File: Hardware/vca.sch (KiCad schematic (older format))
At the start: 41 parts, among them Q1 MMBFJ177, Q2 MMBFJ177, Q3 MMBFJ177, Q4 MMBFJ177, SW1 SW_DPDT_x2, SW2 SW_DPDT_x2, U4 TL074

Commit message: change GNDA to GND nets everywhere. Not using any ADC, so don't need separate digital and analog grounds.
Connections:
- net GNDA is gone; now on net GND: Q1.2 (S), Q2.2 (S), Q3.2 (S), Q4.2 (S), R?.1, R?.1, R?.1, R?.1
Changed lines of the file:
@@
-$EndComp
-$Comp
-L GNDA #PWR37
-U 1 1 5C359DD5
-P 4550 1600
-F 0 "#PWR37" H 4550 1350 50  0001 C CNN
-F 1 "GNDA" H 4550 1450 50  0000 C CNN
-F 2 "" H 4550 1600 50  0001 C CNN
-F 3 "" H 4550 1600 50  0001 C CNN
-	1    4550 1600
-	1    0    0    -1
 $EndComp
 $Comp
@@
 $EndComp
 $Comp
-L GNDA #PWR38
-U 1 1 5C36E8F0
-P 4550 3000
-F 0 "#PWR38" H 4550 2750 50  0001 C CNN
-F 1 "GNDA" H 4550 2850 50  0000 C CNN
-F 2 "" H 4550 3000 50  0001 C CNN
-F 3 "" H 4550 3000 50  0001 C CNN
-	1    4550 3000
-	1    0    0    -1
-$EndComp
-$Comp
 L R R34
 U 1 1 5C36E8F9
@@
 $EndComp
 $Comp
-L GNDA #PWR39
-U 1 1 5C36E9E8
-P 4550 4250
-F 0 "#PWR39" H 4550 4000 50  0001 C CNN
-F 1 "GNDA" H 4550 4100 50  0000 C CNN
-F 2 "" H 4550 4250 50  0001 C CNN
-F 3 "" H 4550 4250 50  0001 C CNN
-	1    4550 4250
-	1    0    0    -1
-$EndComp
-$Comp
 L R R35
 U 1 1 5C36E9F1
@@
 $EndComp
 $Comp
-L GNDA #PWR40
-U 1 1 5C36EAE0
-P 4550 5600
-F 0 "#PWR40" H 4550 5350 50  0001 C CNN
-F 1 "GNDA" H 4550 5450 50  0000 C CNN
-F 2 "" H 4550 5600 50  0001 C CNN
-F 3 "" H 4550 5600 50  0001 C CNN
-	1    4550 5600
-	1    0    0    -1
-$EndComp
-$Comp
 L R R36
 U 1 1 5C36EAE9
@@
 $EndComp
 $Comp
-L GNDA #PWR?
-U 1 1 5C37BC69
-P 6700 1450
-F 0 "#PWR?" H 6700 1200 50  0001 C CNN
-F 1 "GNDA" H 6700 1300 50  0000 C CNN
-F 2 "" H 6700 1450 50  0001 C CNN
-F 3 "" H 6700 1450 50  0001 C CNN
-	1    6700 1450
-	1    0    0    -1
-$EndComp
-$Comp
-L GNDA #PWR?
-U 1 1 5C37BCE0
-P 6700 2850
-F 0 "#PWR?" H 6700 2600 50  0001 C CNN
-F 1 "GNDA" H 6700 2700 50  0000 C CNN
-F 2 "" H 6700 2850 50  0001 C CNN
-F 3 "" H 6700 2850 50  0001 C CNN
-	1    6700 2850
-	1    0    0    -1
-$EndComp
-$Comp
-L GNDA #PWR?
-U 1 1 5C37BD57
-P 6700 4150
-F 0 "#PWR?" H 6700 3900 50  0001 C CNN
-F 1 "GNDA" H 6700 4000 50  0000 C CNN
-F 2 "" H 6700 4150 50  0001 C CNN
-F 3 "" H 6700 4150 50  0001 C CNN
-	1    6700 4150
-	1    0    0    -1
-$EndComp
-$Comp
-L GNDA #PWR?
-U 1 1 5C37BDCE
-P 6700 5450
-F 0 "#PWR?" H 6700 5200 50  0001 C CNN
-F 1 "GNDA" H 6700 5300 50  0000 C CNN
-F 2 "" H 6700 5450 50  0001 C CNN
-F 3 "" H 6700 5450 50  0001 C CNN
-	1    6700 5450
-	1    0    0    -1
-$EndComp
-$Comp
 L R R?
 U 1 1 5C3881CE
@@
 Connection ~ 4550 950
 Wire Wire Line
-	3200 1300 3350 1300
-Wire Wire Line
-	3350 1300 3450 1300
+	3200 1300 3450 1300
 Wire Wire Line
 	2900 1500 3450 1500
@@
 Connection ~ 4550 2350
 Wire Wire Line
-	3300 2700 3400 2700
-Wire Wire Line
-	3400 2700 3450 2700
+	3300 2700 3450 2700
 Wire Wire Line
 	2950 2900 3450 2900
@@
 Connection ~ 4550 3600
 Wire Wire Line
-	3200 3950 3350 3950
-Wire Wire Line
-	3350 3950 3450 3950
+	3200 3950 3450 3950
 Wire Wire Line
 	2850 4150 3450 4150
@@
 Connection ~ 4550 4950
 Wire Wire Line
-	3200 5300 3350 5300
-Wire Wire Line
-	3350 5300 3450 5300
+	3200 5300 3450 5300
 Wire Wire Line
 	2850 5500 3450 5500
@@
 Connection ~ 5150 2350
 Wire Wire Line
-	4250 950  4550 950
-Wire Wire Line
-	4550 950  4800 950
-Wire Wire Line
-	5000 950  5200 950
-Wire Wire Line
-	5200 950  5550 950
-Wire Wire Line
-	5000 2350 5150 2350
-Wire Wire Line
-	5150 2350 5550 2350
-Wire Wire Line
-	4250 2350 4550 2350
-Wire Wire Line
-	4550 2350 4800 2350
-Wire Wire Line
-	4250 3600 4550 3600
-Wire Wire Line
-	4550 3600 4800 3600
-Wire Wire Line
-	5000 3600 5150 3600
-Wire Wire Line
-	5150 3600 5550 3600
-Wire Wire Line
-	4250 4950 4550 4950
-Wire Wire Line
-	4550 4950 4800 4950
-Wire Wire Line
-	5000 4950 5150 4950
-Wire Wire Line
-	5150 4950 5550 4950
-Wire Wire Line
-	6150 1050 6300 1050
-Wire Wire Line
-	6300 1050 6450 1050
-Wire Wire Line
-	6650 1050 6700 1050
-Wire Wire Line
-	6700 1050 6800 1050
+	4250 950  4800 950
+Wire Wire Line
+	5000 950  5550 950
+Wire Wire Line
+	5000 2350 5550 2350
+Wire Wire Line
+	4250 2350 4800 2350
+Wire Wire Line
+	4250 3600 4800 3600
+Wire Wire Line
+	5000 3600 5550 3600
+Wire Wire Line
+	4250 4950 4800 4950
+Wire Wire Line
+	5000 4950 5550 4950
+Wire Wire Line
+	6150 1050 6450 1050
+Wire Wire Line
+	6650 1050 6800 1050
 Wire Wire Line
 	6700 1150 6700 1050
 Connection ~ 6700 1050
 Wire Wire Line
-	6150 2450 6300 2450
-Wire Wire Line
-	6300 2450 6450 2450
-Wire Wire Line
-	6650 2450 6700 2450
-Wire Wire Line
-	6700 2450 6800 2450
+	6150 2450 6450 2450
+Wire Wire Line
+	6650 2450 6800 2450
 Wire Wire Line
 	6700 2550 6700 2450
 Connection ~ 6700 2450
 Wire Wire Line
-	6150 3700 6300 3700
-Wire Wire Line
-	6300 3700 6450 3700
-Wire Wire Line
-	6650 3700 6700 3700
-Wire Wire Line
-	6700 3700 6800 3700
+	6150 3700 6450 3700
+Wire Wire Line
+	6650 3700 6800 3700
 Wire Wire Line
 	6700 3850 6700 3700
 Connection ~ 6700 3700
 Wire Wire Line
-	6150 5050 6300 5050
-Wire Wire Line
-	6300 5050 6450 5050
-Wire Wire Line
-	6650 5050 6700 5050
-Wire Wire Line
-	6700 5050 6800 5050
+	6150 5050 6450 5050
+Wire Wire Line
+	6650 5050 6800 5050
 Wire Wire Line
 	6700 5150 6700 5050
@@
 	1000 1550 1000 1550
 Wire Wire Line
-	1000 1150 1000 1200
-Wire Wire Line
-	1000 1200 1000 1250
+	1000 1150 1000 1250
 Wire Wire Line
 	1000 800  1000 850
@@
 Text Notes 550  2100 0    60   ~ 0
 Determine bias voltage \nunder test, or leave \nunloaded as needed.
+$Comp
+L GND #PWR?
+U 1 1 5C3BC4D7
+P 4550 1600
+F 0 "#PWR?" H 4550 1350 50  0001 C CNN
+F 1 "GND" H 4550 1450 50  0000 C CNN
+F 2 "" H 4550 1600 50  0001 C CNN
+F 3 "" H 4550 1600 50  0001 C CNN
+	1    4550 1600
+	1    0    0    -1
+$EndComp
+$Comp
+L GND #PWR?
+U 1 1 5C3BC62F
+P 6700 1450
+F 0 "#PWR?" H 6700 1200 50  0001 C CNN
+F 1 "GND" H 6700 1300 50  0000 C CNN
+F 2 "" H 6700 1450 50  0001 C CNN
+F 3 "" H 6700 1450 50  0001 C CNN
+	1    6700 1450
+	1    0    0    -1
+$EndComp
+$Comp
+L GND #PWR?
+U 1 1 5C3BC6C4
+P 6700 2850
+F 0 "#PWR?" H 6700 2600 50  0001 C CNN
+F 1 "GND" H 6700 2700 50  0000 C CNN
+F 2 "" H 6700 2850 50  0001 C CNN
+F 3 "" H 6700 2850 50  0001 C CNN
+	1    6700 2850
+	1    0    0    -1
+$EndComp
+$Comp
+L GND #PWR?
+U 1 1 5C3BC759
+P 4550 3000
+F 0 "#PWR?" H 4550 2750 50  0001 C CNN
+F 1 "GND" H 4550 2850 50  0000 C CNN
+F 2 "" H 4550 3000 50  0001 C CNN
+F 3 "" H 4550 3000 50  0001 C CNN
+	1    4550 3000
+	1    0    0    -1
+$EndComp
+$Comp
+L GND #PWR?
+U 1 1 5C3BC7EE
+P 4550 4250
+F 0 "#PWR?" H 4550 4000 50  0001 C CNN
+F 1 "GND" H 4550 4100 50  0000 C CNN
+F 2 "" H 4550 4250 50  0001 C CNN
+F 3 "" H 4550 4250 50  0001 C CNN
+	1    4550 4250
+	1    0    0    -1
+$EndComp
+$Comp
+L GND #PWR?
+U 1 1 5C3BC883
+P 6700 4150
+F 0 "#PWR?" H 6700 3900 50  0001 C CNN
+F 1 "GND" H 6700 4000 50  0000 C CNN
+F 2 "" H 6700 4150 50  0001 C CNN
+F 3 "" H 6700 4150 50  0001 C CNN
+	1    6700 4150
+	1    0    0    -1
+$EndComp
+$Comp
+L GND #PWR?
+U 1 1 5C3BC918
+P 6700 5450
+F 0 "#PWR?" H 6700 5200 50  0001 C CNN
+F 1 "GND" H 6700 5300 50  0000 C CNN
+F 2 "" H 6700 5450 50  0001 C CNN
+F 3 "" H 6700 5450 50  0001 C CNN
+	1    6700 5450
+	1    0    0    -1
+$EndComp
+$Comp
+L GND #PWR?
+U 1 1 5C3BC9AD
+P 4550 5600
+F 0 "#PWR?" H 4550 5350 50  0001 C CNN
+F 1 "GND" H 4550 5450 50  0000 C CNN
+F 2 "" H 4550 5600 50  0001 C CNN
+F 3 "" H 4550 5600 50  0001 C CNN
+	1    4550 5600
+	1    0    0    -1
+$EndComp
 $EndSCHEMATC

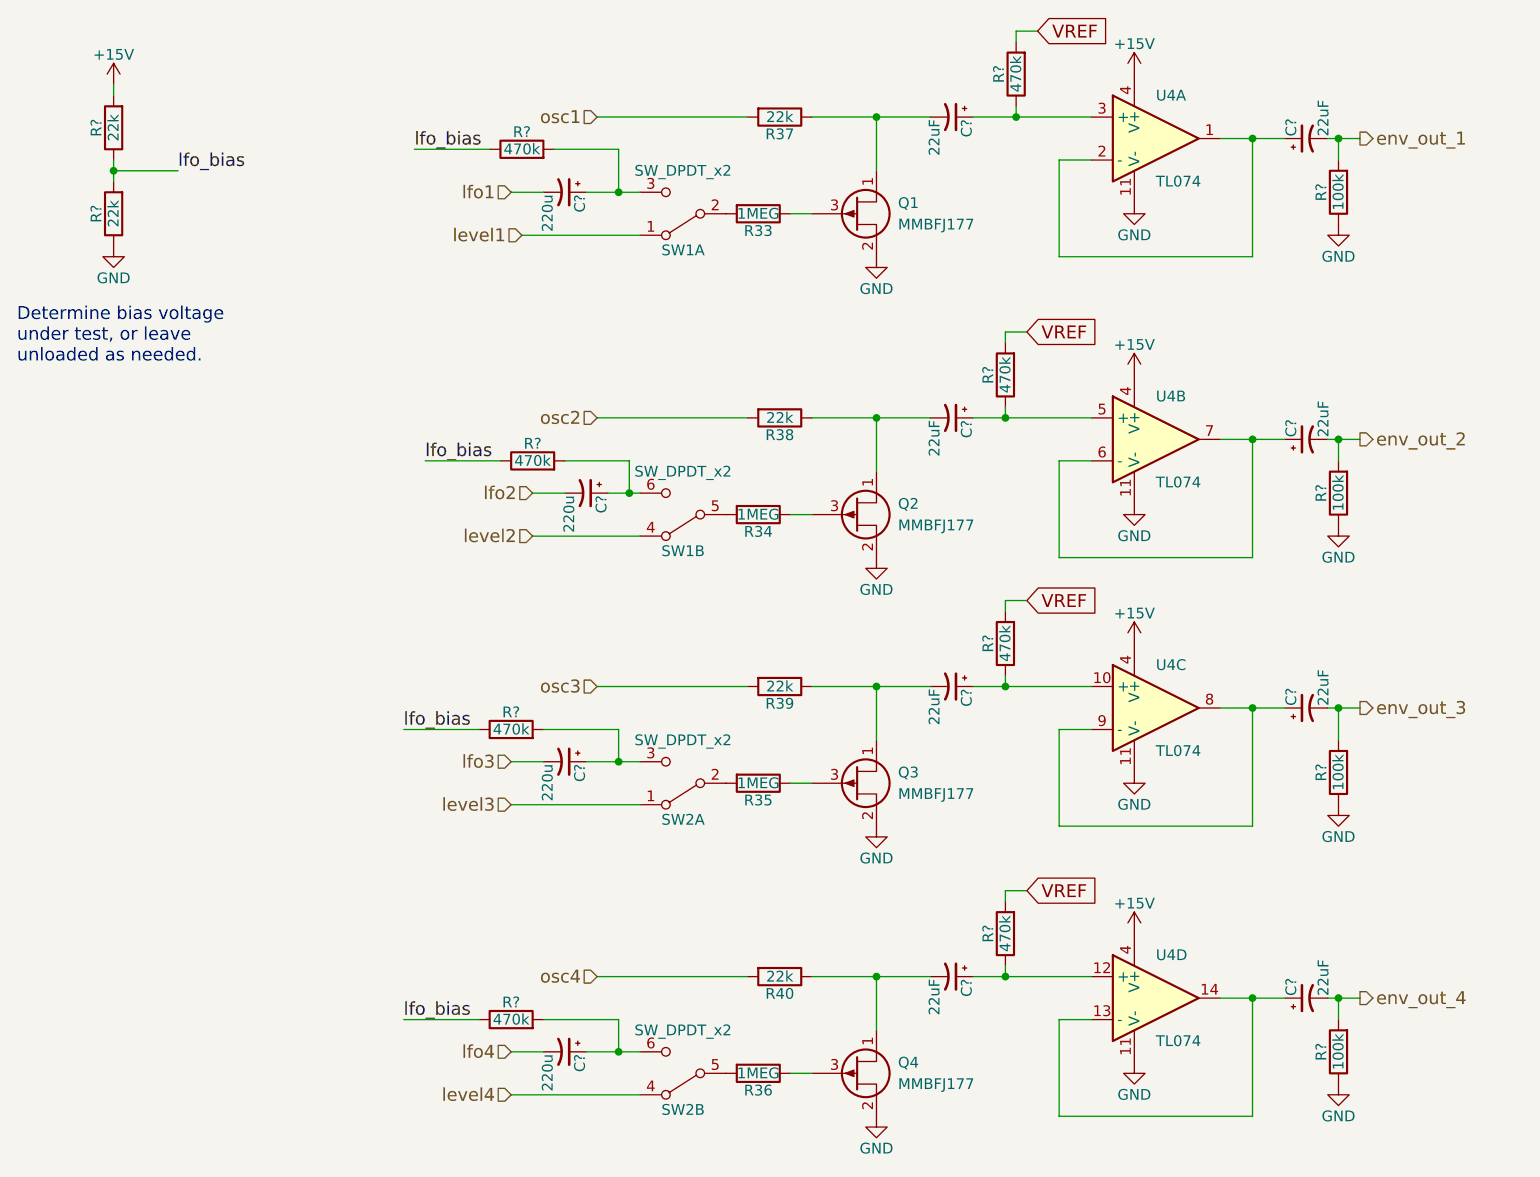
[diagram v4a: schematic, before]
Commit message: add 1Meg + 1nF cap to JFET base to improve biasing linearity.
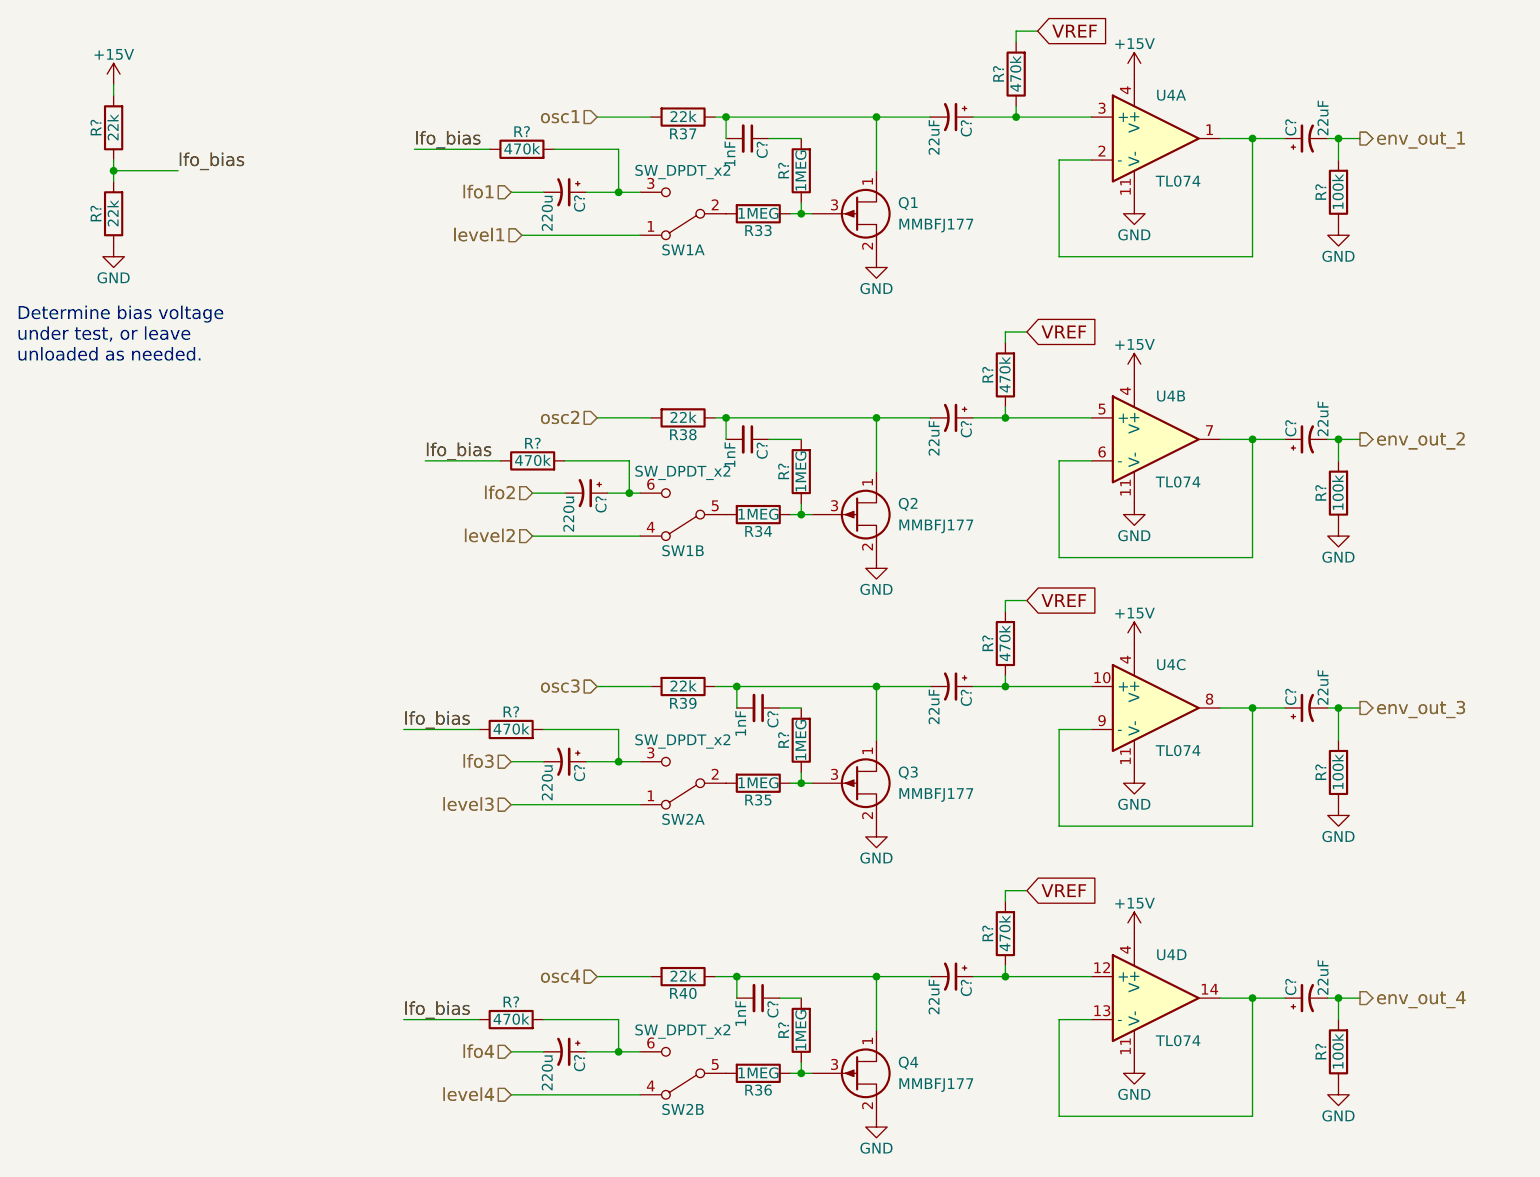
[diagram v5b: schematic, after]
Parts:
- added C? (x4): 1nF, symbol C_Small
- added R? (x4): 1MEG, symbol R
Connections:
- net at C?.2, Q1.1 (D), R37.1: now also C?.2
- net at Q1.3 (G), R33.1: now also R?.1
- net at C?.2, Q2.1 (D), R38.1: now also C?.2
- net at Q2.3 (G), R34.1: now also R?.1
- net at C?.2, Q3.1 (D), R39.1: now also C?.2
- net at Q3.3 (G), R35.1: now also R?.1
- net at C?.2, Q4.1 (D), R40.1: now also C?.2
- net at Q4.3 (G), R36.1: now also R?.1
- new net: C?.1, R?.2 (x4)
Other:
- moved on the sheet: R37, R38, R39, R40

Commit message: mix LFO and Envelope drive signals instead of switching them, and add overall volume mix control to each channel.
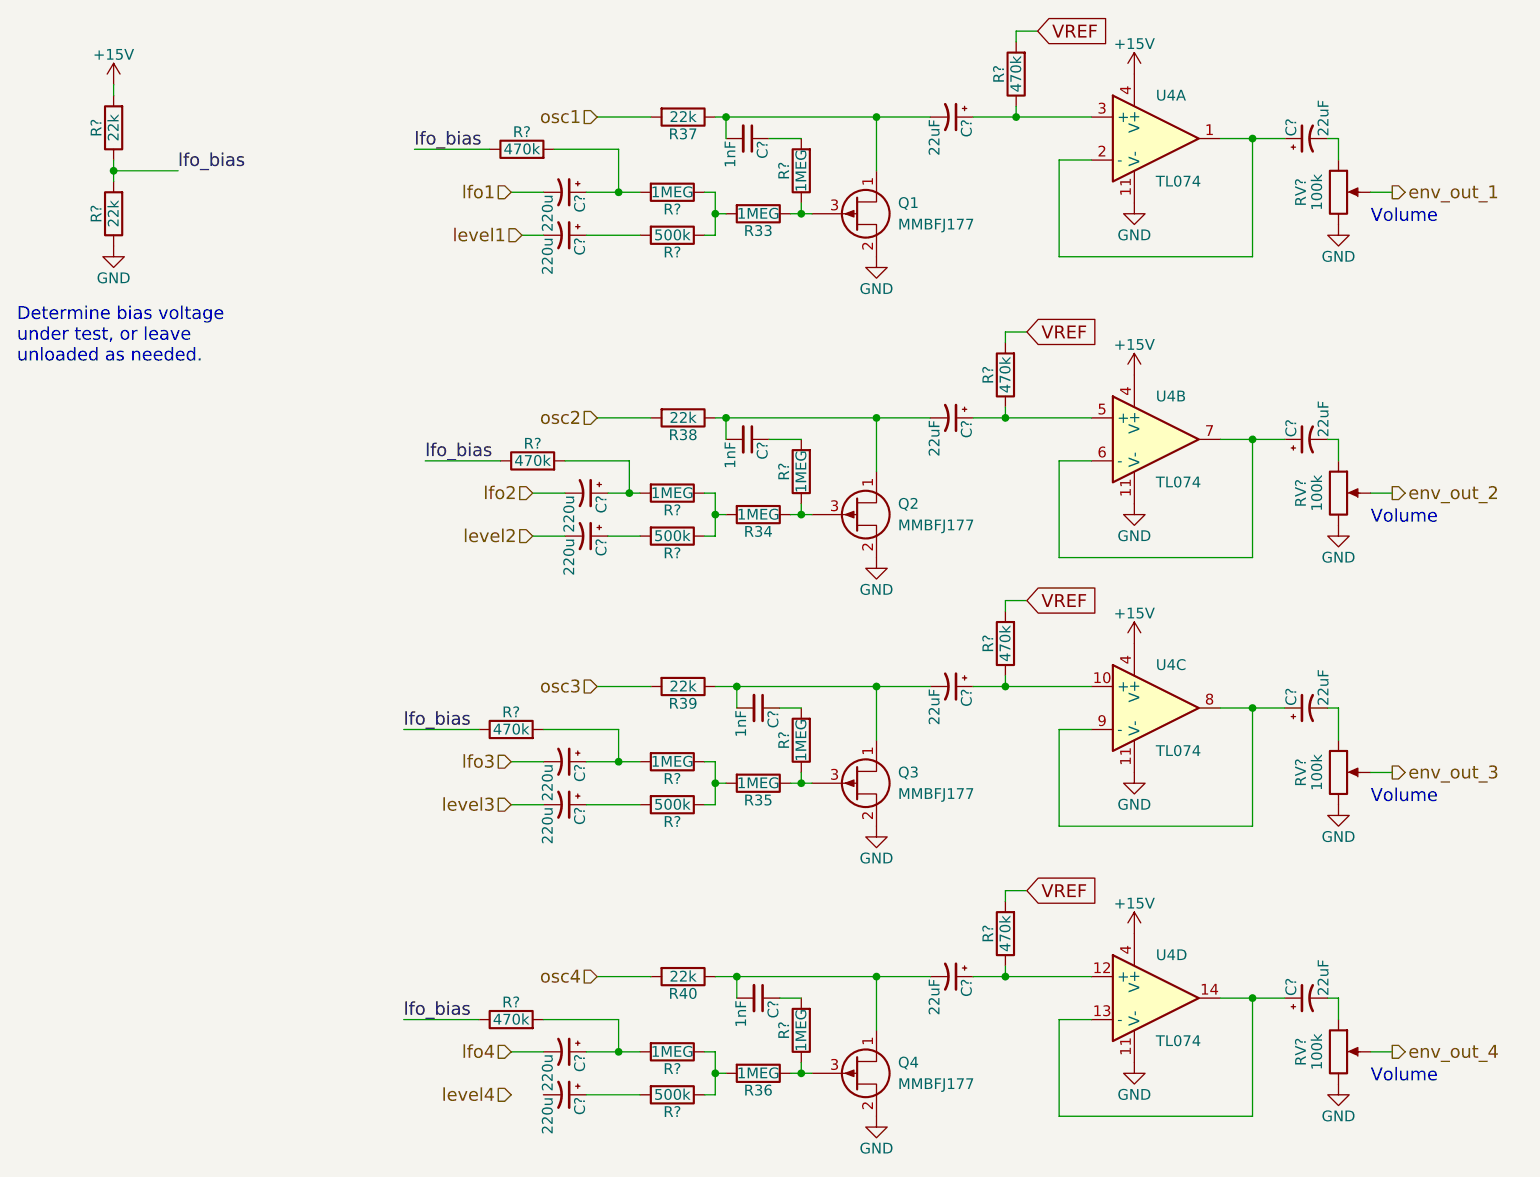
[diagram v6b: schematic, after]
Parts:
- removed R? (x4): 100k, symbol R
- removed SW1, SW2: SW_DPDT_x2, symbol SW_DPDT_x2
- added C? (x4): 220u, symbol CP1_Small
- added R? (x4): 1MEG, symbol R
- added R? (x4): 500k, symbol R
- added RV? (x4): 100k, symbol POT
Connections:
- net GND: now also RV?.3, RV?.3, RV?.3, RV?.3
- net env_out_1: now also RV?.2; no longer C?.2
- net env_out_2: now also RV?.2; no longer C?.2
- net env_out_3: now also RV?.2; no longer C?.2
- net env_out_4: now also RV?.2; no longer C?.2
- net level1: now also C?.2
- net level2: now also C?.2
- net level3: now also C?.2
- net at R33.2: now also R?.1, R?.1
- net at C?.1, R?.2: now also R?.2 (x4)
- net at R34.2: now also R?.1, R?.1
- net at R35.2: now also R?.1, R?.1
- net at R36.2: now also R?.1, R?.1
- new net: C?.2, RV?.1 (x4)
- new net: C?.1, R?.2 (x4)
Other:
- note added: "Volume"
